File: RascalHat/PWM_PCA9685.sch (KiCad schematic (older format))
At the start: 17 parts, among them J10 Conn_01x03, J11 Conn_01x03, J12 Conn_01x03, J13 Conn_01x03, J14 Conn_01x03, J15 Conn_01x03, J16 Conn_01x03, J17 Conn_01x03, J2 Conn_01x03, J3 Conn_01x03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

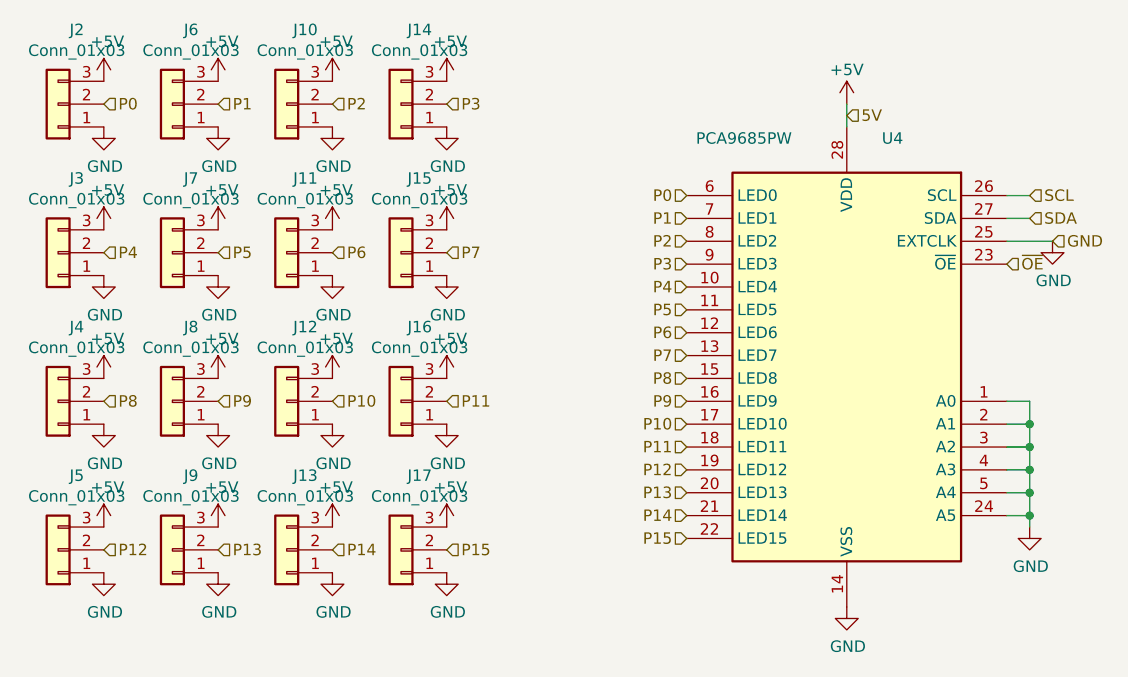
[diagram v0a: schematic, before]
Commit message: schematic done, symbol-footprint done, pcb started
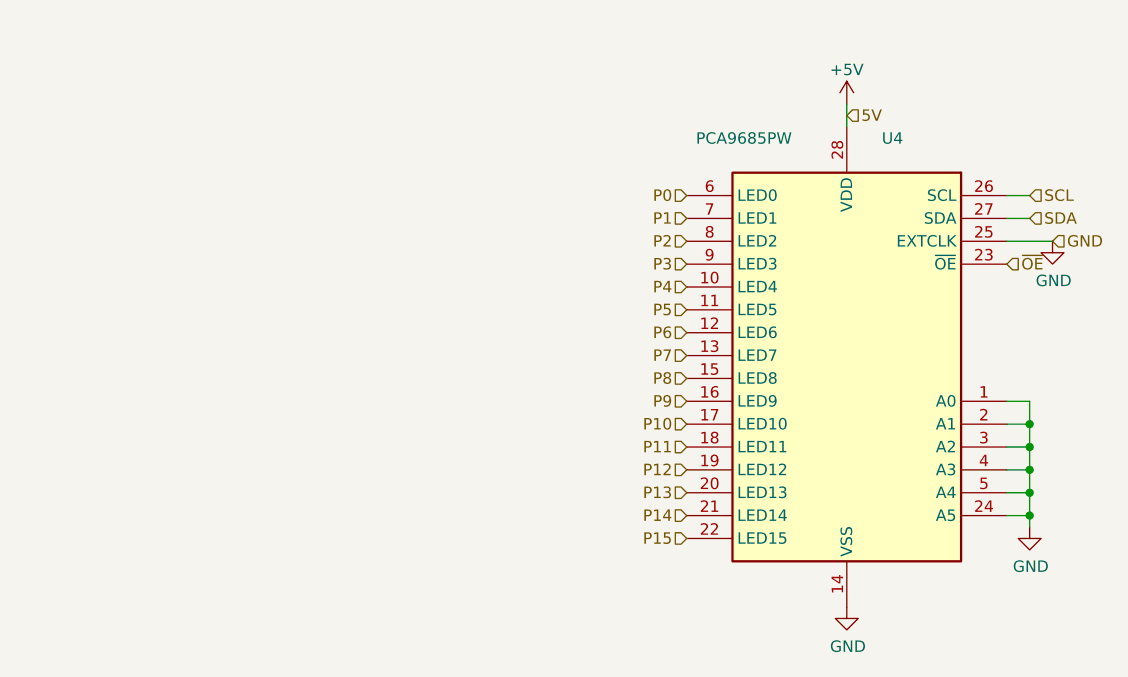
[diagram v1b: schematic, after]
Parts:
- removed J10, J11, J12, J13, J14, J15, J16, J17, J2, J3, J4, J5, J6, J7, J8, J9: Conn_01x03, symbol Connector_Generic:Conn_01x03
